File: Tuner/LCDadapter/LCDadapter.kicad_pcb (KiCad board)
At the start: 2 copper layers, 59 x 56 mm, 30 parts, among them J1 Conn_02x05_Odd_Even, J2 Conn_01x01, J3 Conn_01x01, J4 Conn_01x01, J5 Conn_01x01, Q1 2N3904, SW1 SW_Push, SW2 SW_Push, SW3 SW_Push, SW4 SW_Push, SW5 SW_Push, SW6 SW_Push, U1 PCF8574, U2 LCD-016N002L

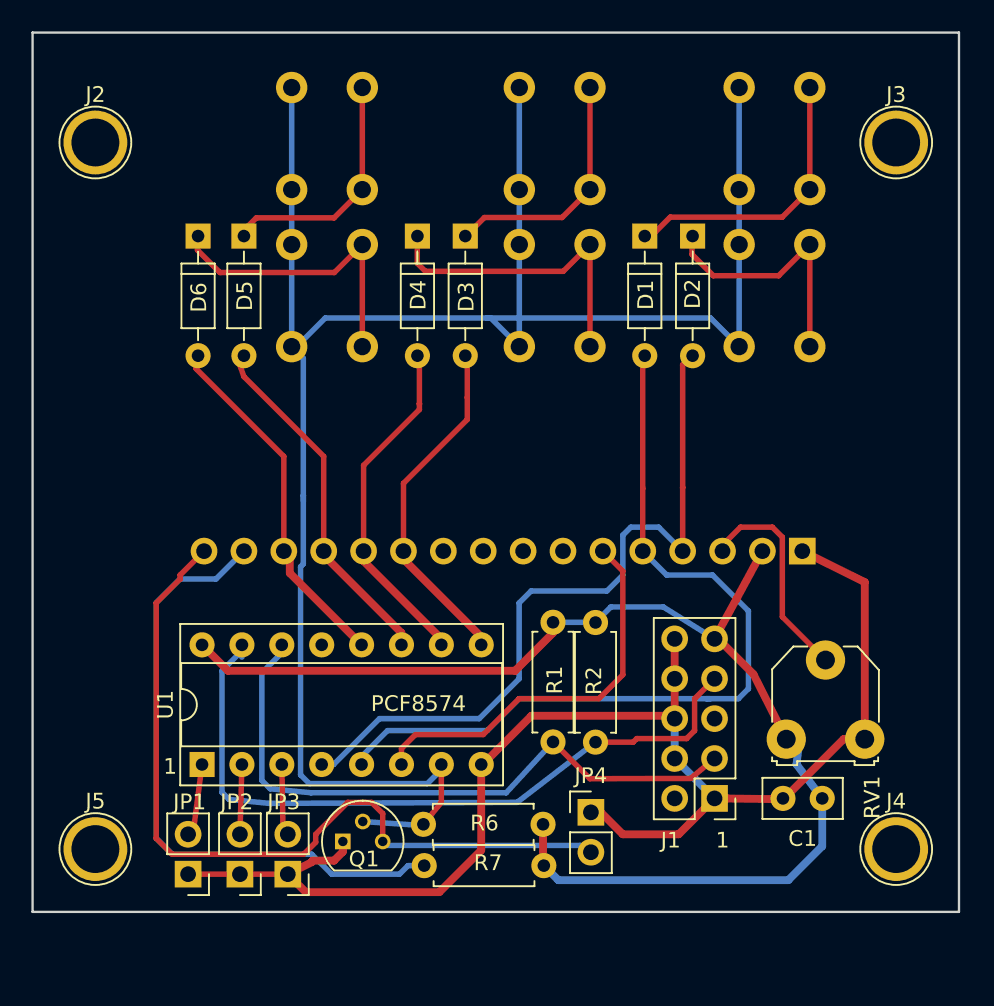
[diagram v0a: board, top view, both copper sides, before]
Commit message: Added some initial I2C user interface stuff
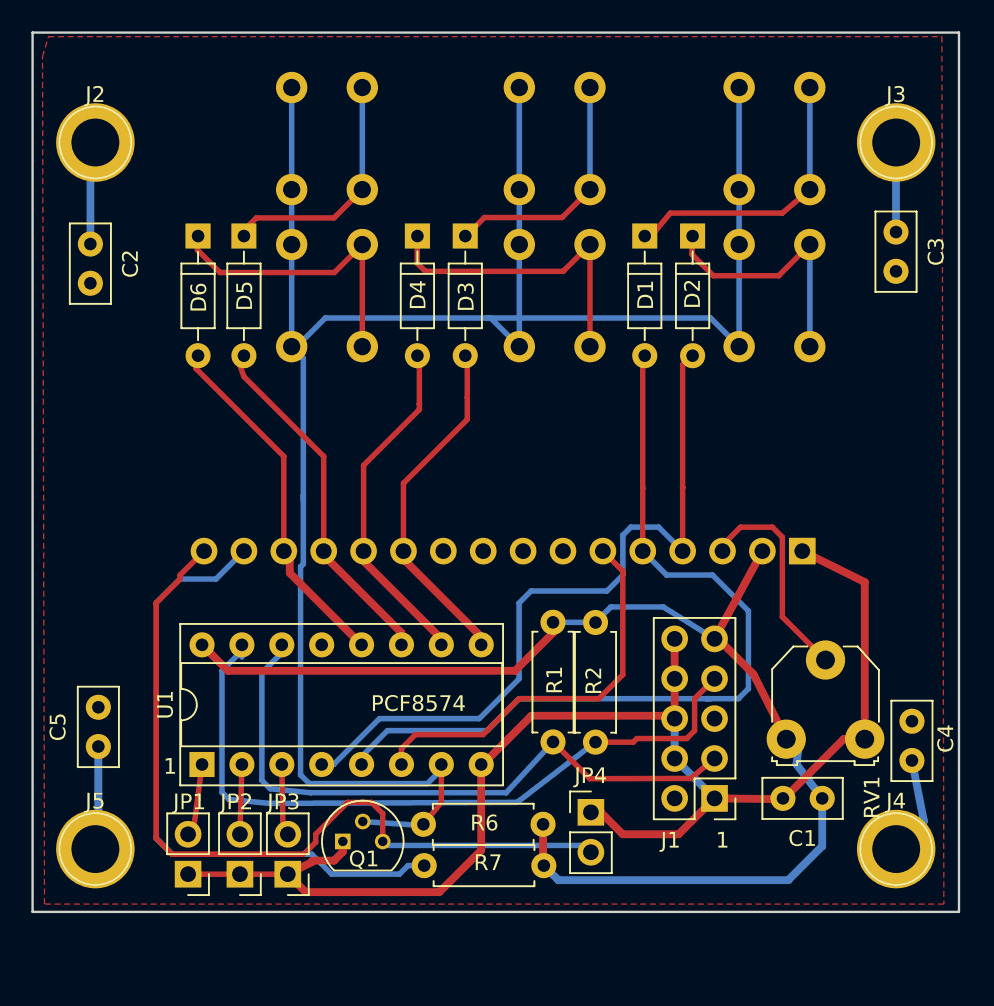
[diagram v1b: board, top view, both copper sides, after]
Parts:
- added C2: 100 nF, Capacitors_THT:C_Disc_D5.0mm_W2.5mm_P2.50mm, F.Cu at (114.7, 45.5)
- added C3: 100 nF, Capacitors_THT:C_Disc_D5.0mm_W2.5mm_P2.50mm, F.Cu at (166.0, 44.7)
- added C4: 100 nF, Capacitors_THT:C_Disc_D5.0mm_W2.5mm_P2.50mm, F.Cu at (167.0, 78.4)
- added C5: 100 nF, Capacitors_THT:C_Disc_D5.0mm_W2.5mm_P2.50mm, F.Cu at (115.2, 77.5)
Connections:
- J2 pad 1: (no net) -> Net-(C2-Pad1)
- J3 pad 1: (no net) -> Net-(C3-Pad1)
- J4 pad 1: (no net) -> Net-(C4-Pad1)
- J5 pad 1: (no net) -> Net-(C5-Pad1)
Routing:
- net Net-(C5-Pad1): track 0.00 -> 6.61 mm
- net Net-(C2-Pad1): track 0.00 -> 6.60 mm
- net Net-(C4-Pad1): track 0.00 -> 6.45 mm
- net Net-(C3-Pad1): track 0.00 -> 5.71 mm
- added copper zone on F.Cu, net GND

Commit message: JLCPCB order 2019-03-25
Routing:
- added copper zone on B.Cu, net GND
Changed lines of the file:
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@@
   )
   (setup
-    (last_trace_width 0.5)
+    (last_trace_width 0.25)
     (user_trace_width 0.35)
     (user_trace_width 0.5)
@@
     (connect_pads (clearance 0.5))
     (min_thickness 0.635)
+    (fill yes (arc_segments 16) (thermal_gap 0.508) (thermal_bridge_width 3))
+    (polygon
+      (pts
+        (xy 112.014 32.258) (xy 168.91 32.258) (xy 169.037 87.503) (xy 111.76 87.503) (xy 111.633 33.528)
+      )
+    )
+  )
+  (zone (net 1) (net_name GND) (layer B.Cu) (hatch edge 0.508)
+    (connect_pads (clearance 0.5))
+    (min_thickness 0.635)

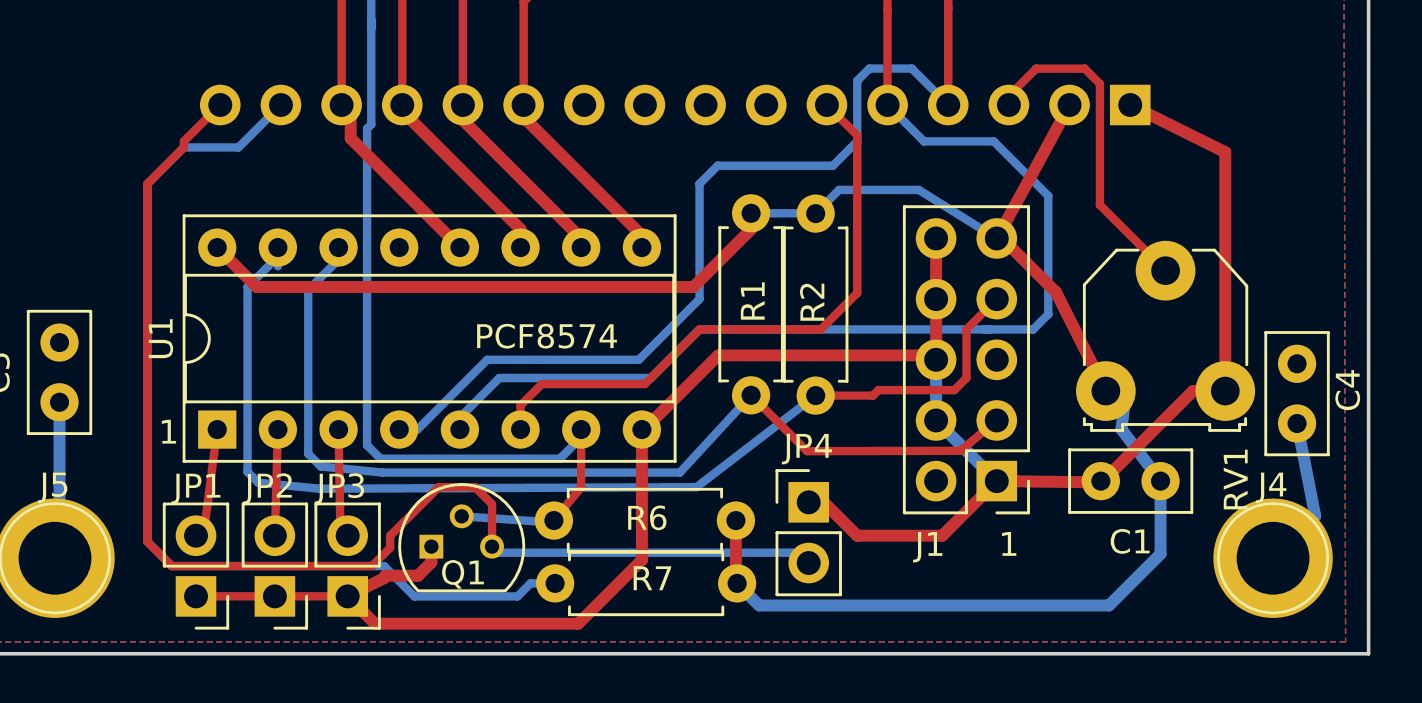
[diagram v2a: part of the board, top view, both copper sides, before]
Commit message: Added nonswitched output to ReversibleSections
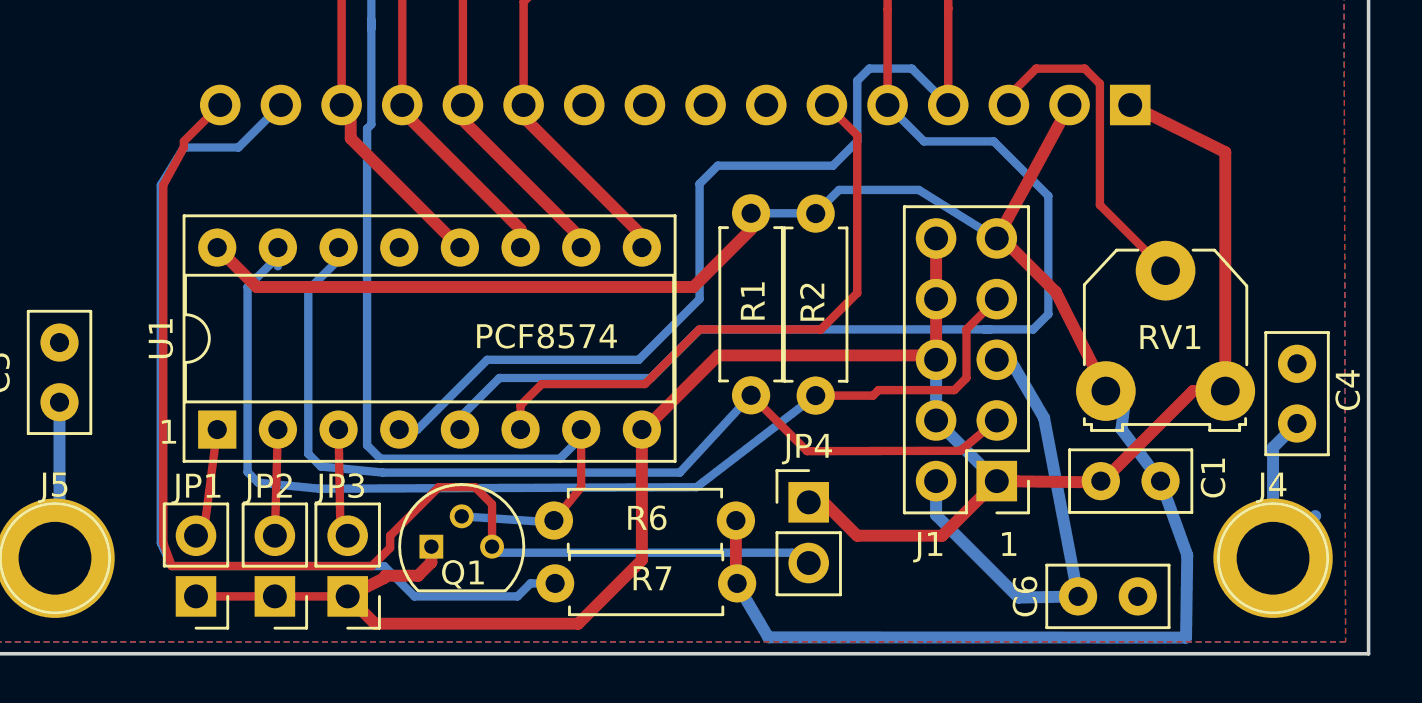
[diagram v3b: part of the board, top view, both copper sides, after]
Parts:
- added C6: 100 nF, Capacitors_THT:C_Disc_D5.0mm_W2.5mm_P2.50mm, F.Cu at (157.8, 85.6)
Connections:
- J1 pad 2: (no net) -> Net-(C6-Pad1)
- J1 pad 5: (no net) -> Net-(C6-Pad1)
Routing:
- net Net-(C6-Pad1): track 0.00 -> 19.8 mm
- net +5V: track 81.1 -> 85.9 mm
- net Net-(C4-Pad1): track 6.45 -> 8.56 mm
- net Net-(JP4-Pad2): track 51.5 -> 50.8 mm
- net Net-(R7-Pad2): track 40.7 -> 40.0 mm
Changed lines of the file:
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@@
 (kicad_pcb (version 4) (host pcbnew 4.0.7)
   (general
-    (links 79)
+    (links 82)
     (no_connects 0)
-    (area 110.252381 31.924999 170.74762 88.075001)
+    (area 110.252381 31.924999 170.74762 89.233)
     (thickness 1.6)
     (drawings 8)
-    (tracks 265)
+    (tracks 272)
     (zones 0)
-    (modules 34)
-    (nets 29)
+    (modules 35)
+    (nets 30)
   )
   (page A4)
   (layers
     (0 F.Cu signal)
-    (31 B.Cu signal)
+    (31 B.Cu signal hide)
     (32 B.Adhes user)
     (33 F.Adhes user)
@@
   )
   (setup
-    (last_trace_width 0.25)
+    (last_trace_width 0.5)
     (user_trace_width 0.35)
     (user_trace_width 0.5)
@@
   (net 27 "Net-(C4-Pad1)")
   (net 28 "Net-(C5-Pad1)")
+  (net 29 "Net-(C6-Pad1)")
   (net_class Default "This is the default net class."
     (clearance 0.2)
@@
     (add_net "Net-(C4-Pad1)")
     (add_net "Net-(C5-Pad1)")
+    (add_net "Net-(C6-Pad1)")
     (add_net "Net-(D1-Pad1)")
     (add_net "Net-(D1-Pad2)")
@@
     (descr "C, Disc series, Radial, pin pitch=2.50mm, , diameter*width=5*2.5mm^2, Capacitor, http://cdn-reichelt.de/documents/datenblatt/B300/DS_KERKO_TC.pdf")
     (tags "C Disc series Radial pin pitch 2.50mm  diameter 5mm width 2.5mm Capacitor")
-    (fp_text reference C1 (at 1.25 -2.56 180) (layer F.SilkS)
+    (fp_text reference C1 (at -2.2352 0.1524 270) (layer F.SilkS)
       (effects (font (size 1 1) (thickness 0.15)))
     )
@@
     (pad 1 thru_hole rect (at 0 0 180) (size 1.7 1.7) (drill 1) (layers *.Cu *.Mask)
       (net 1 GND))
-    (pad 2 thru_hole oval (at 2.54 0 180) (size 1.7 1.7) (drill 1) (layers *.Cu *.Mask))
+    (pad 2 thru_hole oval (at 2.54 0 180) (size 1.7 1.7) (drill 1) (layers *.Cu *.Mask)
+      (net 29 "Net-(C6-Pad1)"))
     (pad 3 thru_hole oval (at 0 2.54 180) (size 1.7 1.7) (drill 1) (layers *.Cu *.Mask)
       (net 14 "Net-(J1-Pad3)"))
     (pad 4 thru_hole oval (at 2.54 2.54 180) (size 1.7 1.7) (drill 1) (layers *.Cu *.Mask)
       (net 1 GND))
-    (pad 5 thru_hole oval (at 0 5.08 180) (size 1.7 1.7) (drill 1) (layers *.Cu *.Mask))
+    (pad 5 thru_hole oval (at 0 5.08 180) (size 1.7 1.7) (drill 1) (layers *.Cu *.Mask)
+      (net 29 "Net-(C6-Pad1)"))
     (pad 6 thru_hole oval (at 2.54 5.08 180) (size 1.7 1.7) (drill 1) (layers *.Cu *.Mask)
       (net 1 GND))
@@
     (descr "Potentiometer, Trimmer, RM-065")
     (tags "Potentiometer Trimmer RM-065")
-    (fp_text reference RV1 (at 5.4737 3.7084 270) (layer F.SilkS)
+    (fp_text reference RV1 (at 2.6964 -2.2224) (layer F.SilkS)
       (effects (font (size 1 1) (thickness 0.15)))
     )
@@
       (net 28 "Net-(C5-Pad1)"))
     (pad 2 thru_hole circle (at 2.5 0 90) (size 1.6 1.6) (drill 0.8) (layers *.Cu *.Mask)
+      (net 1 GND))
+    (model ${KISYS3DMOD}/Capacitors_THT.3dshapes/C_Disc_D5.0mm_W2.5mm_P2.50mm.wrl
+      (at (xyz 0 0 0))
+      (scale (xyz 1 1 1))
+      (rotate (xyz 0 0 0))
+    )
+  )
+  (module Capacitors_THT:C_Disc_D5.0mm_W2.5mm_P2.50mm (layer F.Cu)
+    (at 157.8356 85.598)
+    (descr "C, Disc series, Radial, pin pitch=2.50mm, , diameter*width=5*2.5mm^2, Capacitor, http://cdn-reichelt.de/documents/datenblatt/B300/DS_KERKO_TC.pdf")
+    (tags "C Disc series Radial pin pitch 2.50mm  diameter 5mm width 2.5mm Capacitor")
+    (fp_text reference C6 (at -2.1844 0 90) (layer F.SilkS)
+      (effects (font (size 1 1) (thickness 0.15)))
+    )
+    (fp_text value "100 nF" (at 1.25 2.56) (layer F.Fab)
+      (effects (font (size 1 1) (thickness 0.15)))
+    )
+    (fp_line (start -1.25 -1.25) (end -1.25 1.25) (layer F.Fab) (width 0.1))
+    (fp_line (start -1.25 1.25) (end 3.75 1.25) (layer F.Fab) (width 0.1))
+    (fp_line (start 3.75 1.25) (end 3.75 -1.25) (layer F.Fab) (width 0.1))
+    (fp_line (start 3.75 -1.25) (end -1.25 -1.25) (layer F.Fab) (width 0.1))
+    (fp_line (start -1.31 -1.31) (end 3.81 -1.31) (layer F.SilkS) (width 0.12))
+    (fp_line (start -1.31 1.31) (end 3.81 1.31) (layer F.SilkS) (width 0.12))
+    (fp_line (start -1.31 -1.31) (end -1.31 1.31) (layer F.SilkS) (width 0.12))
+    (fp_line (start 3.81 -1.31) (end 3.81 1.31) (layer F.SilkS) (width 0.12))
+    (fp_line (start -1.6 -1.6) (end -1.6 1.6) (layer F.CrtYd) (width 0.05))
+    (fp_line (start -1.6 1.6) (end 4.1 1.6) (layer F.CrtYd) (width 0.05))
+    (fp_line (start 4.1 1.6) (end 4.1 -1.6) (layer F.CrtYd) (width 0.05))
+    (fp_line (start 4.1 -1.6) (end -1.6 -1.6) (layer F.CrtYd) (width 0.05))
+    (fp_text user %R (at 1.25 0) (layer F.Fab)
+      (effects (font (size 1 1) (thickness 0.15)))
+    )
+    (pad 1 thru_hole circle (at 0 0) (size 1.6 1.6) (drill 0.8) (layers *.Cu *.Mask)
+      (net 29 "Net-(C6-Pad1)"))
+    (pad 2 thru_hole circle (at 2.5 0) (size 1.6 1.6) (drill 0.8) (layers *.Cu *.Mask)
       (net 1 GND))
     (model ${KISYS3DMOD}/Capacitors_THT.3dshapes/C_Disc_D5.0mm_W2.5mm_P2.50mm.wrl
@@
   (segment (start 143.51 82.423) (end 143.51 85.00364) (width 0.5) (layer F.Cu) (net 16) (status 10))
   (segment (start 143.51 85.00364) (end 143.5608 85.05444) (width 0.5) (layer F.Cu) (net 16))
-  (segment (start 143.51 85.00364) (end 144.48536 85.979) (width 0.5) (layer B.Cu) (net 16))
-  (segment (start 144.48536 85.979) (end 159.131 85.979) (width 0.5) (layer B.Cu) (net 16))
-  (segment (start 159.131 85.979) (end 161.29 83.82) (width 0.5) (layer B.Cu) (net 16))
-  (segment (start 161.29 83.82) (end 161.29 80.772) (width 0.5) (layer B.Cu) (net 16))
+  (segment (start 143.51 85.00364) (end 144.86636 87.3125) (width 0.5) (layer B.Cu) (net 16))
+  (segment (start 144.86636 87.3125) (end 162.3568 87.3252) (width 0.5) (layer B.Cu) (net 16))
+  (segment (start 162.3568 87.3252) (end 162.4076 83.8708) (width 0.5) (layer B.Cu) (net 16))
+  (segment (start 162.4076 83.8708) (end 161.29 80.772) (width 0.5) (layer B.Cu) (net 16))
   (segment (start 144.145 69.5579) (end 144.145 70.231) (width 0.5) (layer F.Cu) (net 16))
   (segment (start 144.145 70.231) (end 141.732 72.644) (width 0.5) (layer F.Cu) (net 16))
@@
   (segment (start 122.682 66.802) (end 124.46 65.024) (width 0.35) (layer B.Cu) (net 18))
   (segment (start 120.396 66.802) (end 122.682 66.802) (width 0.35) (layer B.Cu) (net 18))
-  (segment (start 118.872 68.326) (end 120.396 66.802) (width 0.35) (layer B.Cu) (net 18))
-  (segment (start 118.872 83.312) (end 118.872 68.326) (width 0.35) (layer B.Cu) (net 18))
-  (segment (start 119.888 84.328) (end 118.872 83.312) (width 0.35) (layer B.Cu) (net 18))
+  (segment (start 119.4308 68.3768) (end 120.396 66.802) (width 0.35) (layer B.Cu) (net 18))
+  (segment (start 119.4308 83.3628) (end 119.4308 68.3768) (width 0.35) (layer B.Cu) (net 18))
+  (segment (start 119.888 84.328) (end 119.4308 83.3628) (width 0.35) (layer B.Cu) (net 18))
   (segment (start 128.778 84.328) (end 119.888 84.328) (width 0.35) (layer B.Cu) (net 18))
   (segment (start 130.048 85.598) (end 128.778 84.328) (width 0.35) (layer B.Cu) (net 18))
@@
   (segment (start 120.396 66.548) (end 121.92 65.024) (width 0.35) (layer F.Cu) (net 24))
   (segment (start 120.396 66.802) (end 120.396 66.548) (width 0.35) (layer F.Cu) (net 24))
-  (segment (start 118.872 68.326) (end 120.396 66.802) (width 0.35) (layer F.Cu) (net 24))
-  (segment (start 118.872 83.312) (end 118.872 68.326) (width 0.35) (layer F.Cu) (net 24))
-  (segment (start 119.888 84.328) (end 118.872 83.312) (width 0.35) (layer F.Cu) (net 24))
+  (segment (start 119.5324 68.3768) (end 120.396 66.802) (width 0.35) (layer F.Cu) (net 24))
+  (segment (start 119.5324 83.3628) (end 119.5324 68.3768) (width 0.35) (layer F.Cu) (net 24))
+  (segment (start 119.888 84.328) (end 119.5324 83.3628) (width 0.35) (layer F.Cu) (net 24))
   (segment (start 128.27 84.328) (end 119.888 84.328) (width 0.35) (layer F.Cu) (net 24))
   (segment (start 129.032 83.566) (end 128.27 84.328) (width 0.35) (layer F.Cu) (net 24))
@@
   (segment (start 165.989 44.704) (end 165.989 39.011) (width 0.5) (layer B.Cu) (net 26))
   (segment (start 165.989 39.011) (end 166 39) (width 0.5) (layer B.Cu) (net 26))
-  (segment (start 167.005 78.359) (end 167.767 82.233) (width 0.5) (layer B.Cu) (net 27) (status 10))
+  (segment (start 166 84) (end 166 79.364) (width 0.5) (layer B.Cu) (net 27) (status 400000))
+  (segment (start 166 79.364) (end 167.005 78.359) (width 0.5) (layer B.Cu) (net 27) (status 800000))
   (segment (start 167.767 82.233) (end 166 84) (width 0.5) (layer B.Cu) (net 27))
   (segment (start 115.189 77.47) (end 115.189 83.811) (width 0.5) (layer B.Cu) (net 28))
   (segment (start 115.189 83.811) (end 115 84) (width 0.5) (layer B.Cu) (net 28))
+  (segment (start 154.432 75.692) (end 154.9908 75.692) (width 0.5) (layer B.Cu) (net 29))
+  (segment (start 154.9908 75.692) (end 156.4132 78.1304) (width 0.5) (layer B.Cu) (net 29))
+  (segment (start 156.4132 78.1304) (end 157.8356 85.598) (width 0.5) (layer B.Cu) (net 29) (status 20))
+  (segment (start 151.892 80.772) (end 151.892 82.1944) (width 0.5) (layer B.Cu) (net 29))
+  (segment (start 155.3464 85.6488) (end 157.8356 85.598) (width 0.5) (layer B.Cu) (net 29) (status 20))
+  (segment (start 151.892 82.1944) (end 155.3464 85.6488) (width 0.5) (layer B.Cu) (net 29))
   (zone (net 1) (net_name GND) (layer F.Cu) (hatch edge 0.508)
     (connect_pads (clearance 0.5))

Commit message: LCDAdapter added dual polarity set I2C address
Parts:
- JP1, JP2, JP3: value Jumper -> Jumper_NC_Dual; footprint Pin_Headers:Pin_Header_Straight_1x02_Pitch2.54mm -> Pin_Headers:Pin_Header_Straight_1x03_Pitch2.54mm
- moved C1 44.9 mm to (117.5, 70.5), turned to 90 degrees
- moved C6 2.58 mm to (160.3, 85.0), turned to 90 degrees
- moved JP1 2.41 mm to (120.1, 83.3), turned to 0 degrees
- moved JP2 2.30 mm to (124.0, 83.3), turned to 0 degrees
- moved JP3 2.30 mm to (127.5, 83.3), turned to 0 degrees
- moved C5 2.29 mm to (115.2, 79.8)
- moved J4 2.00 mm to (166.0, 86.0)
- moved J5 2.00 mm to (115.0, 86.0)
- moved Q1 1.32 mm to (130.8, 84.8)
- moved R7 1.31 mm to (143.5, 86.4)
- moved C4 1.28 mm to (167.1, 79.6)
- moved R6 0.64 mm to (143.5, 83.1)
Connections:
- JP1 pad 1: GND -> +5V
- JP2 pad 1: GND -> +5V
- JP3 pad 1: GND -> +5V
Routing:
- net +5V: track 85.9 -> 129.4 mm
- net GND: track 91.5 -> 61.2 mm
- net Net-(JP3-Pad2): track 4.57 -> 9.21 mm
- net Net-(JP2-Pad2): track 4.45 -> 8.94 mm
- net Net-(JP4-Pad2): track 50.8 -> 46.7 mm
- net Net-(JP1-Pad2): track 4.63 -> 8.52 mm
- net Net-(C4-Pad1): track 8.56 -> 4.68 mm
- net Net-(R7-Pad2): track 40.0 -> 42.5 mm
- net Net-(C5-Pad1): track 6.61 -> 4.32 mm
- net Net-(C6-Pad1): track 19.8 -> 20.6 mm
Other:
- board size 59 x 56 mm -> 58.2 x 59.7 mm
- board text added: "A0"
- board text added: "A1"
- board text added: "A2"
- board text added: "H"
- board text added: "L"
